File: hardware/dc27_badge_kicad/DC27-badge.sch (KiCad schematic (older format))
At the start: 28 parts, among them J101 Conn_ARM_JTAG_SWD_10, J102 ShittyAddOnL, J103 ShittyAddOnR, J104 Conn_02x20_Odd_Even, J105 Conn_01x02_Female, SW101 UP, SW102 DN, SW103 LEFT, SW104 RIGHT, SW105 A, SW106 B, SW107 ENTER, SW108 RESET, U101 BMD-340-A-R, Y101 32.768Khz XTAL

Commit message: clean up fp libraries
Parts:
- removed U101: BMD-340-A-R, BMD-340-A-R:RIGADO_BMD-340-A-R, symbol DC27-peripheral-cache:BMD-340-A-R
- added U100: BMD-340-A-R-DC27-peripheral-cache, RIGADO_BMD-340-A-R, symbol DC27-badge-rescue:BMD-340-A-R-DC27-peripheral-cache
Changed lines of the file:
@@
 Text Notes 5750 650  0    50   ~ 10
 Dual Shitty Add On’s!
-$Comp
-L DC27-peripheral-cache:+3.3V #PWR0101
-U 1 1 5BA9C6B3
-P 7200 800
-F 0 "#PWR0101" H 7200 650 50  0001 C CNN
-F 1 "+3.3V" H 7215 973 50  0000 C CNN
-F 2 "" H 7200 800 50  0001 C CNN
-F 3 "" H 7200 800 50  0001 C CNN
-	1    7200 800
-	1    0    0    -1
-$EndComp
 Wire Wire Line
 	7200 800  7200 1050
@@
 Wire Wire Line
 	9100 2800 9850 2800
-$Comp
-L DC27-peripheral-cache:+3.3V #PWR0105
-U 1 1 5BA9D13E
-P 10650 2650
-F 0 "#PWR0105" H 10650 2500 50  0001 C CNN
-F 1 "+3.3V" H 10665 2823 50  0000 C CNN
-F 2 "" H 10650 2650 50  0001 C CNN
-F 3 "" H 10650 2650 50  0001 C CNN
-	1    10650 2650
-	1    0    0    -1
-$EndComp
 Wire Wire Line
 	10650 2650 10650 2800
@@
 Wire Wire Line
 	1150 5200 1150 5300
-$Comp
-L DC27-peripheral-cache:+3.3V #PWR0107
-U 1 1 5BB1B8C1
-P 1150 3600
-F 0 "#PWR0107" H 1150 3450 50  0001 C CNN
-F 1 "+3.3V" H 1165 3773 50  0000 C CNN
-F 2 "" H 1150 3600 50  0001 C CNN
-F 3 "" H 1150 3600 50  0001 C CNN
-	1    1150 3600
-	1    0    0    -1
-$EndComp
-Wire Wire Line
-	1150 3600 1150 3650
 Text GLabel 2300 4200 2    50   Output ~ 0
 ~RESET_TGTMCU
@@
 Wire Wire Line
 	1750 3650 1150 3650
-Connection ~ 1150 3650
-Wire Wire Line
-	1150 3650 1150 3900
 Text Notes 550  3350 0    50   ~ 10
 PROGRAMMING HEADER
@@
 Text GLabel 6150 3350 2    50   Output ~ 0
 SDT_SPI_SCK
-$Comp
-L DC27-peripheral-cache:BMD-340-A-R U101
-U 1 1 5BB20AB5
-P 5000 3850
-F 0 "U101" H 5000 4000 50  0000 C CNN
-F 1 "BMD-340-A-R" H 5000 3850 50  0000 C CNN
-F 2 "BMD-340-A-R:RIGADO_BMD-340-A-R" H 4600 1800 50  0001 L BNN
-F 3 "Rigado" H 4750 5800 50  0001 L BNN
-F 4 "Bluetooth Low Energy 5.0 Module" H 4750 5650 50  0001 L BNN "Field4"
-F 5 "BMD-340-A-R" H 4750 5900 50  0001 L BNN "Field6"
-	1    5000 3850
-	1    0    0    -1
-$EndComp
 Wire Wire Line
 	5750 3350 6150 3350
@@
 Wire Wire Line
 	5750 2750 6150 2750
+$Comp
+L power:+3.3V #PWR0105
+U 1 1 5C58C1FA
+P 7200 800
+F 0 "#PWR0105" H 7200 650 50  0001 C CNN
+F 1 "+3.3V" H 7215 973 50  0000 C CNN
+F 2 "" H 7200 800 50  0001 C CNN
+F 3 "" H 7200 800 50  0001 C CNN
+	1    7200 800
+	1    0    0    -1
+$EndComp
+$Comp
+L DC27-badge-rescue:BMD-340-A-R-DC27-peripheral-cache U100
+U 1 1 5C59EA27
+P 5000 3850
+F 0 "U100" H 5025 5565 50  0000 C CNN
+F 1 "BMD-340-A-R-DC27-peripheral-cache" H 5025 5474 50  0000 C CNN
+F 2 "RIGADO_BMD-340-A-R" H 5600 1750 50  0001 L BNN
+F 3 "Rigado" H 4550 5700 50  0001 L BNN
+F 4 "Bluetooth Low Energy 5.0 Module" H 4550 5550 50  0001 L BNN "Field4"
+F 5 "BMD-340-A-R" H 4550 5800 50  0001 L BNN "Field6"
+	1    5000 3850
+	1    0    0    -1
+$EndComp
+Wire Wire Line
+	1150 3600 1150 3650
+Connection ~ 1150 3650
+Wire Wire Line
+	1150 3650 1150 3900
+$Comp
+L power:+3.3V #PWR0107
+U 1 1 5C5B1B5F
+P 1150 3600
+F 0 "#PWR0107" H 1150 3450 50  0001 C CNN
+F 1 "+3.3V" H 1165 3773 50  0000 C CNN
+F 2 "" H 1150 3600 50  0001 C CNN
+F 3 "" H 1150 3600 50  0001 C CNN
+	1    1150 3600
+	1    0    0    -1
+$EndComp
+$Comp
+L power:+3.3V #PWR0101
+U 1 1 5C5B1CAA
+P 10650 2650
+F 0 "#PWR0101" H 10650 2500 50  0001 C CNN
+F 1 "+3.3V" H 10665 2823 50  0000 C CNN
+F 2 "" H 10650 2650 50  0001 C CNN
+F 3 "" H 10650 2650 50  0001 C CNN
+	1    10650 2650
+	1    0    0    -1
+$EndComp
 $EndSCHEMATC

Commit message: add gerbers for prototype
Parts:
- removed J105: Conn_01x02_Female, Connector_PinHeader_1.00mm:PinHeader_1x02_P1.00mm_Horizontal, symbol Connector:Conn_01x02_Female
- removed TP107: XTAL0, TestPoint:TestPoint_Pad_D2.0mm, symbol Connector:TestPoint
- removed TP108: XTAL1, TestPoint:TestPoint_Pad_D2.0mm, symbol Connector:TestPoint
- J104: footprint Connector_PinSocket_2.54mm:PinSocket_2x20_P2.54mm_Vertical_SMD -> samtec:SAMTEC-SSM-120-X-DV
- TP104: value SDT_SPI_SCK -> DISP_SCLK
- TP105: value DISP_MOSI -> DISP_MISO
- U100: footprint RIGADO_BMD-340-A-R -> BMD-340-A-R:RIGADO_BMD-340-A-R
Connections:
- wire segments 241 -> 237
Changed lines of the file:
@@
 F 0 "J104" H 10100 4817 50  0000 C CNN
 F 1 "Conn_02x20_Odd_Even" H 10100 4726 50  0000 C CNN
-F 2 "Connector_PinSocket_2.54mm:PinSocket_2x20_P2.54mm_Vertical_SMD" H 10050 3700 50  0001 C CNN
-F 3 "~" H 10050 3700 50  0001 C CNN
+F 2 "samtec:SAMTEC-SSM-120-X-DV" H 10050 3700 50  0001 C CNN
+F 3 "-" H 10050 3700 50  0001 C CNN
 	1    10050 3700
 	1    0    0    -1
@@
 Text GLabel 6150 3150 2    50   Output ~ 0
 I2S_MCK
-$Comp
-L Connector:TestPoint TP108
-U 1 1 5BD7474F
-P 9550 5450
-F 0 "TP108" H 9608 5570 50  0000 L CNN
-F 1 "XTAL1" H 9608 5479 50  0000 L CNN
-F 2 "TestPoint:TestPoint_Pad_D2.0mm" H 9750 5450 50  0001 C CNN
-F 3 "~" H 9750 5450 50  0001 C CNN
-	1    9550 5450
-	1    0    0    -1
-$EndComp
-Wire Wire Line
-	9550 5450 9550 5600
-$Comp
-L Connector:TestPoint TP107
-U 1 1 5BD7D538
-P 8800 5450
-F 0 "TP107" H 8600 5550 50  0000 L CNN
-F 1 "XTAL0" H 8500 5450 50  0000 L CNN
-F 2 "TestPoint:TestPoint_Pad_D2.0mm" H 9000 5450 50  0001 C CNN
-F 3 "~" H 9000 5450 50  0001 C CNN
-	1    8800 5450
-	1    0    0    -1
-$EndComp
-Wire Wire Line
-	8800 5450 8800 5600
 Wire Notes Line
 	7400 500  7400 6550
@@
 P 8250 3950
 F 0 "TP104" H 8308 4070 50  0000 L CNN
-F 1 "SDT_SPI_SCK" H 8308 3979 50  0000 L CNN
+F 1 "DISP_SCLK" H 8308 3979 50  0000 L CNN
 F 2 "TestPoint:TestPoint_Pad_D2.0mm" H 8450 3950 50  0001 C CNN
 F 3 "~" H 8450 3950 50  0001 C CNN
@@
 P 8200 4350
 F 0 "TP105" H 8258 4470 50  0000 L CNN
-F 1 "DISP_MOSI" H 8258 4379 50  0000 L CNN
+F 1 "DISP_MISO" H 8258 4379 50  0000 L CNN
 F 2 "TestPoint:TestPoint_Pad_D2.0mm" H 8400 4350 50  0001 C CNN
 F 3 "~" H 8400 4350 50  0001 C CNN
@@
 Wire Wire Line
 	3450 4450 4300 4450
-$Comp
-L Connector:Conn_01x02_Female J105
-U 1 1 5C18A401
-P 2600 3400
-F 0 "J105" H 2627 3376 50  0000 L CNN
-F 1 "Conn_01x02_Female" H 2627 3285 50  0000 L CNN
-F 2 "Connector_PinHeader_1.00mm:PinHeader_1x02_P1.00mm_Horizontal" H 2600 3400 50  0001 C CNN
-F 3 "~" H 2600 3400 50  0001 C CNN
-	1    2600 3400
-	1    0    0    -1
-$EndComp
 Text Notes 1850 3300 0    50   ~ 10
 NFC antenna connector - DNP
-Text GLabel 2300 3400 0    50   BiDi ~ 0
-NFC_ANT0
-Text GLabel 2300 3500 0    50   BiDi ~ 0
-NFC_ANT1
-Wire Wire Line
-	2300 3500 2400 3500
-Wire Wire Line
-	2400 3400 2300 3400
 Wire Wire Line
 	5900 2200 5900 2350
@@
 Text Notes 7350 7500 0    50   ~ 0
 DC27 BADGE -  CPU, DISPLAY, USER INTERFACE - REV 1
-$Comp
-L Connector_Generic:Conn_02x02_Odd_Even J102
-U 1 1 5C536AAC
-P 6700 1050
-F 0 "J102" H 6750 1267 50  0000 C CNN
-F 1 "ShittyAddOnL" H 6750 1176 50  0000 C CNN
-F 2 "Connector_PinSocket_2.54mm:PinSocket_2x02_P2.54mm_Vertical_SMD" H 6700 1050 50  0001 C CNN
-F 3 "~" H 6700 1050 50  0001 C CNN
-	1    6700 1050
-	1    0    0    -1
-$EndComp
 Wire Notes Line
 	7400 1950 5700 1950
@@
 F 0 "U100" H 5025 5565 50  0000 C CNN
 F 1 "BMD-340-A-R-DC27-peripheral-cache" H 5025 5474 50  0000 C CNN
-F 2 "RIGADO_BMD-340-A-R" H 5600 1750 50  0001 L BNN
+F 2 "BMD-340-A-R:RIGADO_BMD-340-A-R" H 5600 1750 50  0001 L BNN
 F 3 "Rigado" H 4550 5700 50  0001 L BNN
 F 4 "Bluetooth Low Energy 5.0 Module" H 4550 5550 50  0001 L BNN "Field4"
@@
 	1    0    0    -1
 $EndComp
+$Comp
+L Connector_Generic:Conn_02x02_Odd_Even J102
+U 1 1 5C536AAC
+P 6700 1050
+F 0 "J102" H 6750 1267 50  0000 C CNN
+F 1 "ShittyAddOnL" H 6750 1176 50  0000 C CNN
+F 2 "Connector_PinSocket_2.54mm:PinSocket_2x02_P2.54mm_Vertical_SMD" H 6700 1050 50  0001 C CNN
+F 3 "~" H 6700 1050 50  0001 C CNN
+	1    6700 1050
+	1    0    0    -1
+$EndComp

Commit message: check in all datasheets, BOM tools, and start to get first fab together
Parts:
- Y101: footprint Crystal:Crystal_SMD_MicroCrystal_CC4V-T1A-2Pin_5.0x1.9mm -> Crystal:Crystal_SMD_MicroCrystal_CC7V-T1A-2Pin_3.2x1.5mm
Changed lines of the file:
@@
 F 0 "Y101" H 9200 5868 50  0000 C CNN
 F 1 "32.768Khz XTAL" H 9200 5777 50  0000 C CNN
-F 2 "Crystal:Crystal_SMD_MicroCrystal_CC4V-T1A-2Pin_5.0x1.9mm" H 9200 5600 50  0001 C CNN
+F 2 "Crystal:Crystal_SMD_MicroCrystal_CC7V-T1A-2Pin_3.2x1.5mm" H 9200 5600 50  0001 C CNN
 F 3 "~" H 9200 5600 50  0001 C CNN
 	1    9200 5600

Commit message: add AST-01078 3d model and kicad footprint, check in current budget, update charging circut to MCP73833 instead of MCP73831:
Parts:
- J101: symbol Connector:Conn_ARM_JTAG_SWD_10 -> DC27-badge-rescue:Conn_ARM_JTAG_SWD_10-Connector
- SW101, SW102, SW103, SW104, SW105, SW106, SW107, SW108: symbol MF_Switches:TACT_4.2MM -> DC27-badge-rescue:TACT_4.2MM-MF_Switches
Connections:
- net labels removed: NFC_ANT0, NFC_ANT1
- wire segments 237 -> 235
- no-connect marks 44 -> 46
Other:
- note added: "NFC Antenna\nNot used\n"
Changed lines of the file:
@@
 EESchema Schematic File Version 4
 LIBS:DC27-badge-cache
-EELAYER 26 0
+EELAYER 29 0
 EELAYER END
 $Descr A4 11693 8268
@@
 	4950 6150 4950 6400
 $Comp
-L MF_Switches:TACT_4.2MM SW101
+L DC27-badge-rescue:TACT_4.2MM-MF_Switches SW101
 U 1 1 5BA99567
 P 7800 1600
@@
 $EndComp
 $Comp
-L MF_Switches:TACT_4.2MM SW102
+L DC27-badge-rescue:TACT_4.2MM-MF_Switches SW102
 U 1 1 5BA995D9
 P 8250 1600
@@
 $EndComp
 $Comp
-L MF_Switches:TACT_4.2MM SW104
+L DC27-badge-rescue:TACT_4.2MM-MF_Switches SW104
 U 1 1 5BA9965D
 P 9150 1600
@@
 $EndComp
 $Comp
-L MF_Switches:TACT_4.2MM SW105
+L DC27-badge-rescue:TACT_4.2MM-MF_Switches SW105
 U 1 1 5BA99697
 P 9600 1600
@@
 $EndComp
 $Comp
-L MF_Switches:TACT_4.2MM SW103
+L DC27-badge-rescue:TACT_4.2MM-MF_Switches SW103
 U 1 1 5BA9B5C7
 P 8750 1600
@@
 $EndComp
 $Comp
-L MF_Switches:TACT_4.2MM SW106
+L DC27-badge-rescue:TACT_4.2MM-MF_Switches SW106
 U 1 1 5BA9B5F5
 P 10100 1600
@@
 NoConn ~ 10350 4500
 $Comp
-L Connector:Conn_ARM_JTAG_SWD_10 J101
+L DC27-badge-rescue:Conn_ARM_JTAG_SWD_10-Connector J101
 U 1 1 5BB15372
 P 1150 4500
@@
 PROGRAMMING HEADER
 $Comp
-L MF_Switches:TACT_4.2MM SW107
+L DC27-badge-rescue:TACT_4.2MM-MF_Switches SW107
 U 1 1 5BB3B53E
 P 10550 1600
@@
 Wire Wire Line
 	4100 4150 4300 4150
-Text GLabel 4100 4250 0    50   BiDi ~ 0
-NFC_ANT0
-Text GLabel 4100 4350 0    50   BiDi ~ 0
-NFC_ANT1
-Wire Wire Line
-	4100 4350 4300 4350
-Wire Wire Line
-	4300 4250 4100 4250
 Text GLabel 3450 4650 0    50   Output ~ 0
 SD_CS
@@
 	8200 4950 8150 4950
 $Comp
-L MF_Switches:TACT_4.2MM SW108
+L DC27-badge-rescue:TACT_4.2MM-MF_Switches SW108
 U 1 1 5C05F22F
 P 11000 1600
@@
 	1    0    0    -1
 $EndComp
+NoConn ~ 4300 4350
+NoConn ~ 4300 4250
+Text Notes 3800 4400 0    50   ~ 0
+NFC Antenna\nNot used\n
 $EndSCHEMATC

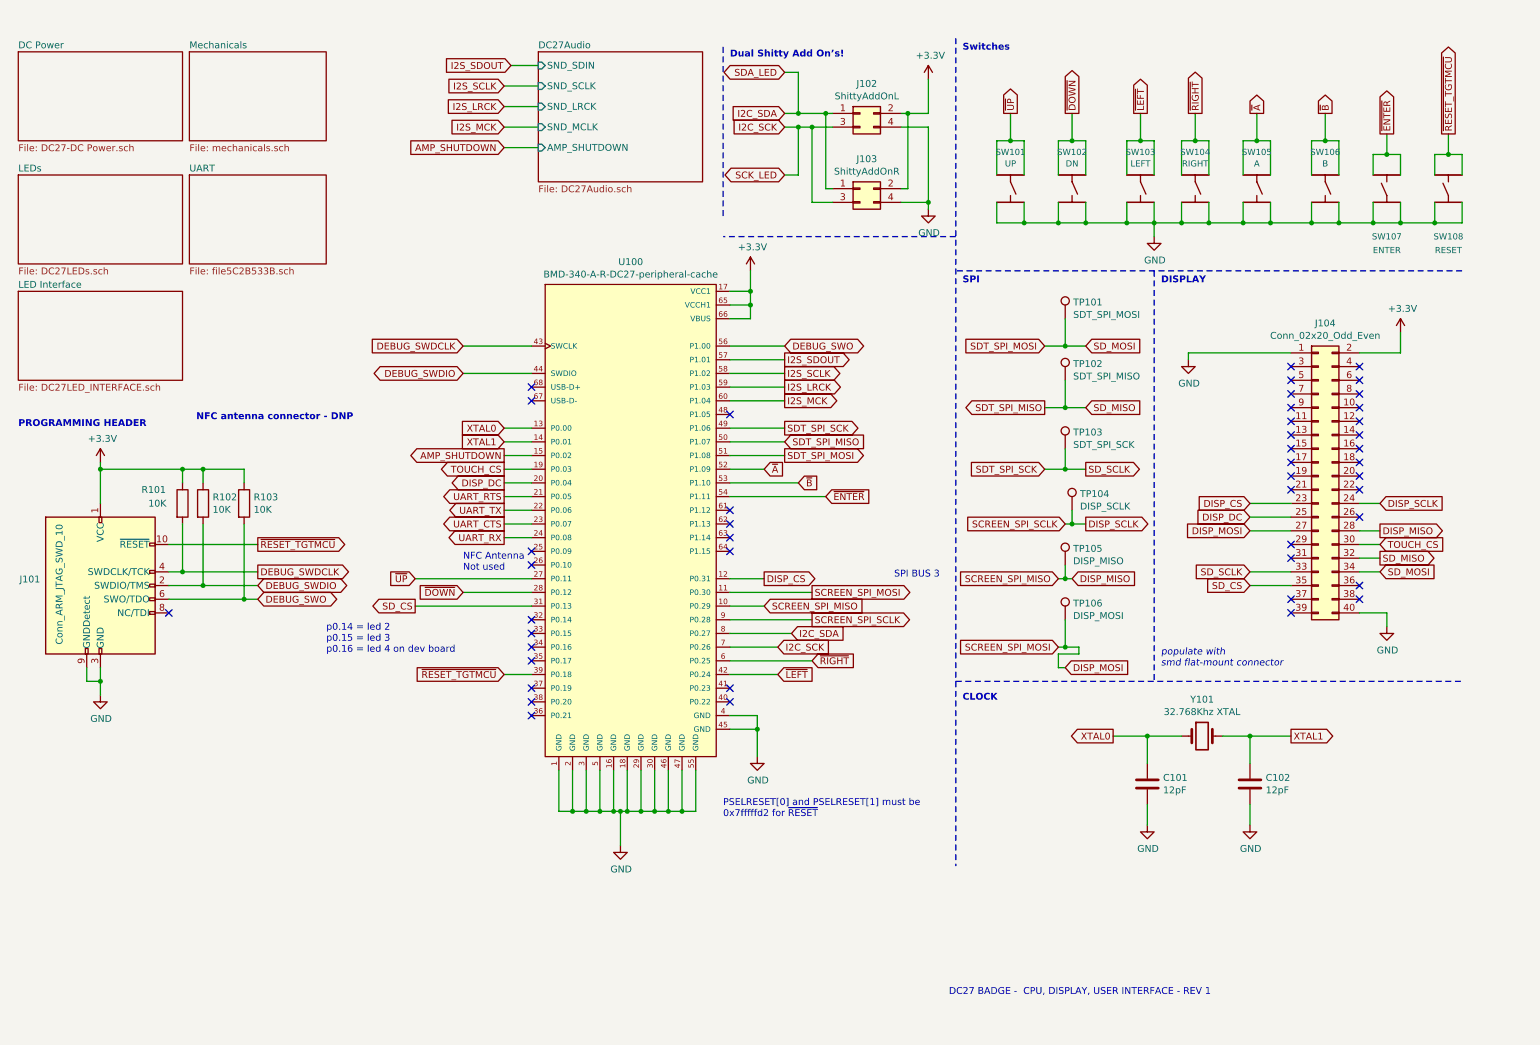
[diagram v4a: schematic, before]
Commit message: add in the new buttons and joystick interrupts, make new schematic for joypads, update the pcb (not done)
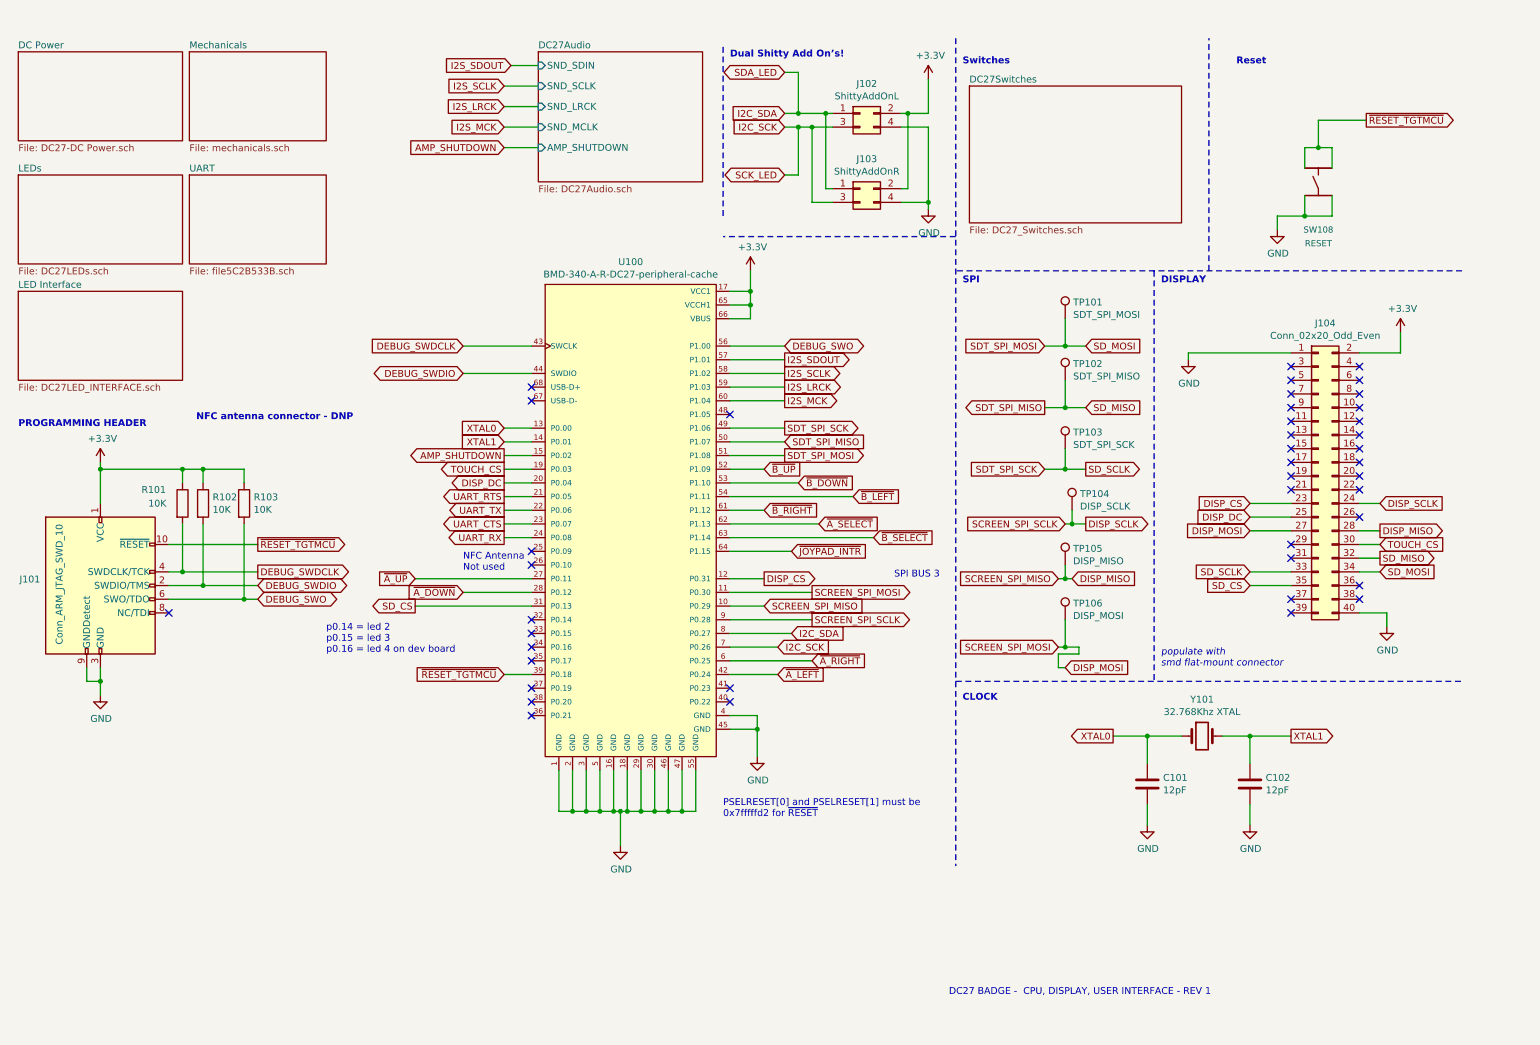
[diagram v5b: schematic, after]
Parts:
- removed SW101: UP, MF_Switches:MF_Switches-TACT4.2MM, symbol DC27-badge-rescue:TACT_4.2MM-MF_Switches
- removed SW102: DN, MF_Switches:MF_Switches-TACT4.2MM, symbol DC27-badge-rescue:TACT_4.2MM-MF_Switches
- removed SW103: LEFT, MF_Switches:MF_Switches-TACT4.2MM, symbol DC27-badge-rescue:TACT_4.2MM-MF_Switches
- removed SW104: RIGHT, MF_Switches:MF_Switches-TACT4.2MM, symbol DC27-badge-rescue:TACT_4.2MM-MF_Switches
- removed SW105: A, MF_Switches:MF_Switches-TACT4.2MM, symbol DC27-badge-rescue:TACT_4.2MM-MF_Switches
- removed SW106: B, MF_Switches:MF_Switches-TACT4.2MM, symbol DC27-badge-rescue:TACT_4.2MM-MF_Switches
- removed SW107: ENTER, MF_Switches:MF_Switches-TACT4.2MM, symbol DC27-badge-rescue:TACT_4.2MM-MF_Switches
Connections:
- net ~B_RIGHT: now reaches U100.61 (P1.12)
- net ~A_SELECT: now reaches U100.62 (P1.13)
- net ~B_SELECT: now reaches U100.63 (P1.14)
- net ~JOYPAD_INTR: now reaches U100.64 (P1.15)
- net ~A renamed ~B_UP
- net ~B renamed ~B_DOWN
- net ~DOWN renamed ~A_DOWN
- net ~ENTER renamed ~B_LEFT
- net ~LEFT renamed ~A_LEFT
- net ~RIGHT renamed ~A_RIGHT
- net ~UP renamed ~A_UP
- no-connect marks 46 -> 42
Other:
- note added: "Reset\n"
- moved on the sheet: SW108

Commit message: Check in V2 of the board. 0 unconnected nets, joypads on pcb
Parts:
- J102, J103: footprint Connector_PinSocket_2.54mm:PinSocket_2x02_P2.54mm_Vertical_SMD -> Connector_PinSocket_2.54mm:PinSocket_2x03_P2.54mm_Vertical; symbol Connector_Generic:Conn_02x02_Odd_Even -> Connector_Generic:Conn_02x03_Odd_Even
- TP101, TP102, TP103, TP104, TP105, TP106: footprint TestPoint:TestPoint_Pad_D2.0mm -> Connector_PinHeader_2.54mm:PinHeader_1x01_P2.54mm_Vertical
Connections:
- net +3V3: now also J102.1 (Pin_1), J103.1 (Pin_1); no longer J102.2 (Pin_2), J103.2 (Pin_2)
- net GND: now also J102.2 (Pin_2), J103.2 (Pin_2); no longer J102.4 (Pin_4), J103.4 (Pin_4)
- net I2C_SCK: now also J102.4 (Pin_4), J103.4 (Pin_4); no longer J102.3 (Pin_3), J103.3 (Pin_3)
- net I2C_SDA: now also J102.3 (Pin_3), J103.3 (Pin_3); no longer J102.1 (Pin_1), J103.1 (Pin_1)
- net SAO_GPIO1: now reaches U100.32 (P0.14)
- net SAO_GPIO1: now also J102.5 (Pin_5), J103.5 (Pin_5)
- net SAO_GPIO2: now reaches U100.33 (P0.15)
- net SAO_GPIO2: now also J102.6 (Pin_6), J103.6 (Pin_6)
- no-connect marks 42 -> 40
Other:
- moved on the sheet: SW108

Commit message: PROTOV2 OFF TO MACROFAB
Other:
- note added: "Note that the keyed side of the\nSAO connector must face off the board.\nThe left hand side shall be rotated\n-180 degress."
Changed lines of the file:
@@
 	1    0    0    -1
 $EndComp
+Text Notes 550  7650 0    50   ~ 0
+Note that the keyed side of the\nSAO connector must face off the board.\nThe left hand side shall be rotated\n-180 degress.
 $EndSCHEMATC
